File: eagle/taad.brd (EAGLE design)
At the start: 81.2 x 74.3 mm, 49 parts, among them IC1 LD117AS33TR, Q1 16 MHz, X1 MINI-USB-32005-201

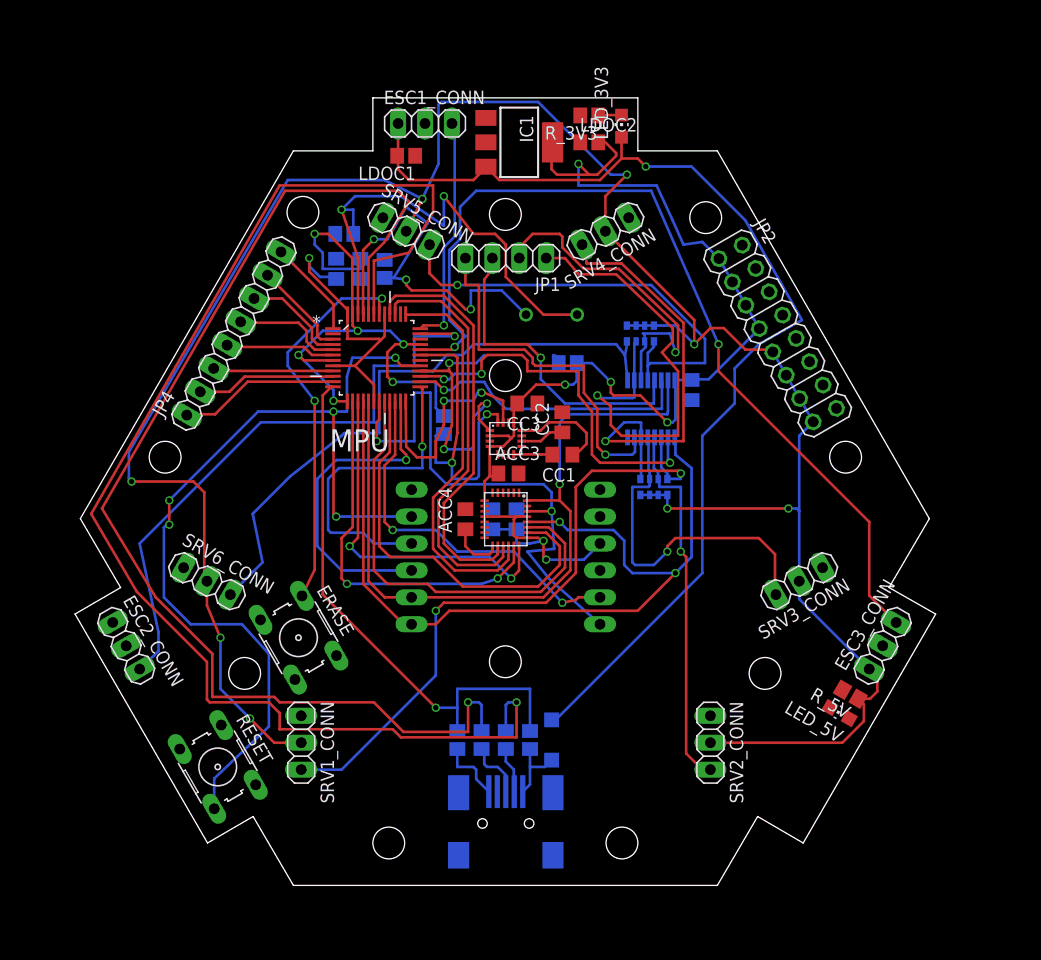
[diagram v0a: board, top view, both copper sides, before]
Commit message: Updated with recommendations from Hannes regarding capacitors on supply and some diagnostic leds. New routing of components
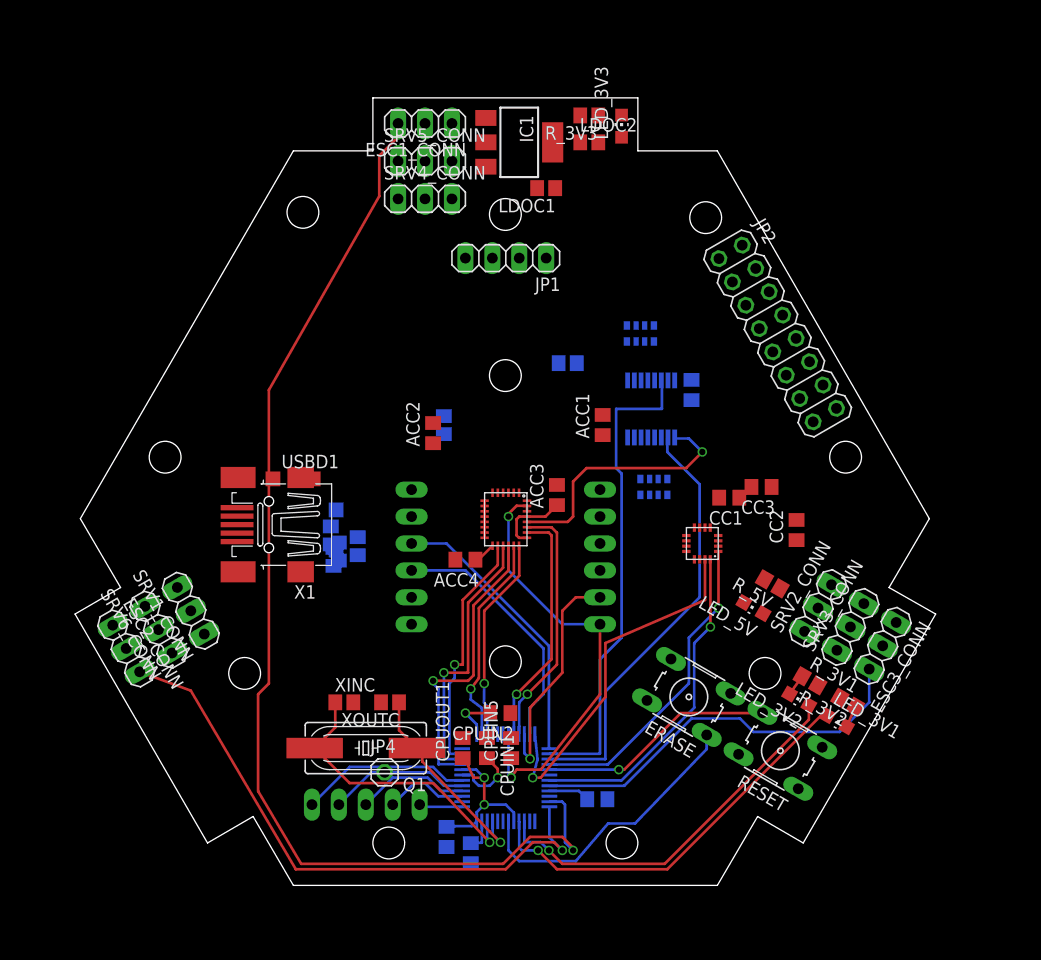
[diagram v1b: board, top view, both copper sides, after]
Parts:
- removed CPUC1: 2.2µ, rcl:C0805
- removed CPUC2: 10µ, rcl:C0805
- added CPUIN1, CPUIN2, CPUIN3, CPUIN4, CPUOUT1: 100n, rcl:C0805
- added CPUIN5: 10µ, rcl:C0805
- added CPUOUT2: 2.2µ, rcl:C0805
- added JP3: (no value), pinhead:1X05
- added LED_3V1, LED_3V2: (no value), led:CHIP-LED0805
- added R_3V1, R_3V2: 160, resistor:R0805
- added USBD1: (no value), diode:SOD123
- JP4: device pinhead:1X08 -> pinhead:1X01
- Q1: device crystal:HC49/S -> crystal:HC49UP
- moved RESET 53.1 mm to (66.5, 12.7), turned to 150 degrees
- moved Q1 44.5 mm to (27.4, 13.0), flipped to the top
- moved XINC 44.2 mm to (25.4, 17.3), flipped to the top
- moved JP4 43.8 mm to (29.2, 10.7), turned to 0 degrees
- moved MPU 41.5 mm to (40.6, 10.2), flipped to the bottom, turned to 180 degrees
- moved XOUTC 40.9 mm to (29.7, 17.3), flipped to the top, turned to 180 degrees
- moved ERASE 37.3 mm to (57.9, 17.8), turned to 150 degrees
- moved X1 36.0 mm to (18.3, 34.0), flipped to the top, turned to 180 degrees
- moved USBD 28.4 mm to (24.6, 33.5)
- moved USBR3 24.5 mm to (26.7, 32.0)
- moved CC2 24.3 mm to (68.1, 33.5)
- moved USBR2 24.0 mm to (24.1, 33.0)
- moved USBR1 23.7 mm to (24.4, 31.0)
- moved CC3 23.5 mm to (64.8, 37.6)
- moved COMPASS 21.0 mm to (59.2, 32.3), turned to 180 degrees
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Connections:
- removed net AD0: JP4.3, MPU.9
- removed net AD1: JP4.2, MPU.10
- removed net AD2: JP4.1, MPU.11
- new net N$1: ESC1_CONN.1, USBD1.A
- new net N$11: JP4.1, MPU.37
- new net N$2: LED_3V2.A, MPU.39
- new net N$6: LED_3V1.A, MPU.40
- new net N$8: LED_3V2.C, R_3V1.1
- new net N$9: LED_3V1.C, R_3V2.1
- net +3V3: now also CPUIN1.2, CPUIN2.2, CPUIN3.2, CPUIN4.2, CPUIN5.1, ERASE.3; no longer CPUC2.1
- net AD3: now also JP3.4; no longer JP4.7
- net AD4: now also JP3.3; no longer JP4.6
- net AD5: now also JP3.2; no longer JP4.5
- net AD6: now also JP3.1; no longer JP4.4
- net ADVREF: now also JP3.5; no longer JP4.8
- net DEN_G: now also MPU.11; no longer MPU.40
- net ESC1: now also MPU.35; no longer MPU.36
- net ESC2: now also MPU.36; no longer MPU.35
- net GND: now also CPUIN1.1, CPUIN2.1, CPUIN3.1, CPUIN4.1, CPUIN5.2, CPUOUT1.2, CPUOUT2.2, R_3V1.2, R_3V2.2; no longer CPUC1.2, CPUC2.2, ERASE.3
- net INT1_G: now also MPU.9; no longer MPU.37
- net INT2_G: now also MPU.10; no longer MPU.39
- net N$24: now also USBD1.C; no longer ESC1_CONN.1
- net NPCS0: now also GYRO/ACCEL.22; no longer GYRO/ACCEL.23
- net NPCS2: now also GYRO/ACCEL.23; no longer GYRO/ACCEL.22
- net VDDCORE: now also CPUOUT1.1, CPUOUT2.1; no longer CPUC1.1
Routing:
- net +5V: track 224.2 -> 0.00 mm, vias 8 -> 0
- net +3V3: track 171.5 -> 28.9 mm, vias 12 -> 2
- net DDM: track 125.5 -> 0.00 mm, vias 1 -> 0
- net DDP: track 112.2 -> 0.00 mm, vias 1 -> 0
- net N$24: track 103.2 -> 0.00 mm, vias 1 -> 0
- net ESC1: track 21.9 -> 108.5 mm
- net SDA: track 68.9 -> 0.00 mm, vias 1 -> 0
- net RESET: track 87.8 -> 22.3 mm, vias 5 -> 1
- net SRV1: track 61.9 -> 0.00 mm, vias 2 -> 0
- net SRV6: track 58.2 -> 0.00 mm
- net SCK: track 81.8 -> 24.4 mm, vias 2 -> 1
- net USB_CONNECTED: track 52.0 -> 0.00 mm, vias 1 -> 0
- net ESC3: track 85.7 -> 37.6 mm, vias 2 -> 0
- net IO1: track 45.0 -> 0.00 mm, vias 1 -> 0
- net SRV5: track 43.0 -> 0.00 mm, vias 1 -> 0
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
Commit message: Routed everything
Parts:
- removed JP2: (no value), pinhead:2X08
- added JP5, JP6: (no value), pinhead:2X04
- moved TWI_DR 35.1 mm to (64.3, 24.4), turned to 0 degrees
- moved USBR2 29.6 mm to (26.7, 3.56), turned to 270 degrees
- moved TWI_CR 28.8 mm to (64.3, 26.7)
- moved JP4 28.6 mm to (57.7, 7.62)
- moved USBR1 28.2 mm to (23.4, 2.79), turned to 180 degrees
- moved USBD1 25.4 mm to (31.8, 61.2)
- moved X1 20.8 mm to (11.9, 14.2), turned to 30 degrees
- moved CC2 12.9 mm to (55.4, 31.5), turned to 270 degrees
- moved USBR3 10.8 mm to (22.4, 22.1), flipped to the top
- moved USBD 10.4 mm to (25.4, 23.1), flipped to the top
- moved ACC1 10.0 mm to (40.4, 39.9)
- moved CC1 9.54 mm to (53.1, 32.5), turned to 90 degrees
- moved USBR4 5.68 mm to (22.4, 26.4), flipped to the top, turned to 270 degrees
- moved CC3 5.61 mm to (64.3, 32.0)
- moved LED_3V3 5.49 mm to (48.5, 67.1), turned to 270 degrees
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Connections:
- net +3V3: now also JP5.1, JP5.3, JP5.5, JP5.7; no longer JP2.1, JP2.3, JP2.5, JP2.7
- net +5V: now also JP6.1, JP6.3, JP6.5, JP6.7; no longer JP2.11, JP2.13, JP2.15, JP2.9
- net GND: now also JP5.2, JP5.4, JP5.6, JP5.8, JP6.2, JP6.4, JP6.6, JP6.8; no longer JP2.10, JP2.12, JP2.14, JP2.16, JP2.2, JP2.4, JP2.6, JP2.8
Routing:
- net +3V3: track 28.9 -> 208.1 mm, vias 2 -> 8
- net +5V: track 0.00 -> 161.3 mm, vias 0 -> 3
- net SDA: track 0.00 -> 82.9 mm, vias 0 -> 1
- net SRV1: track 0.00 -> 65.6 mm, vias 0 -> 1
- net SRV6: track 0.00 -> 65.3 mm, vias 0 -> 3
- net N$24: track 0.00 -> 64.7 mm
- net SCK: track 24.4 -> 81.7 mm, vias 1 -> 2
- net RESET: track 22.3 -> 72.0 mm
- net SRV4: track 0.00 -> 45.6 mm, vias 0 -> 2
- net IO3: track 0.00 -> 35.3 mm
- net SRV3: track 0.00 -> 34.9 mm, vias 0 -> 1
- net SRV5: track 0.00 -> 33.7 mm
- net VDDCORE: track 16.9 -> 44.2 mm, vias 2 -> 4
- net SRV2: track 0.00 -> 26.6 mm, vias 0 -> 1
- net IO4: track 0.00 -> 26.4 mm, vias 0 -> 1
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- added copper zone on layer 1, net GND
- added copper zone on layer 16, net GND

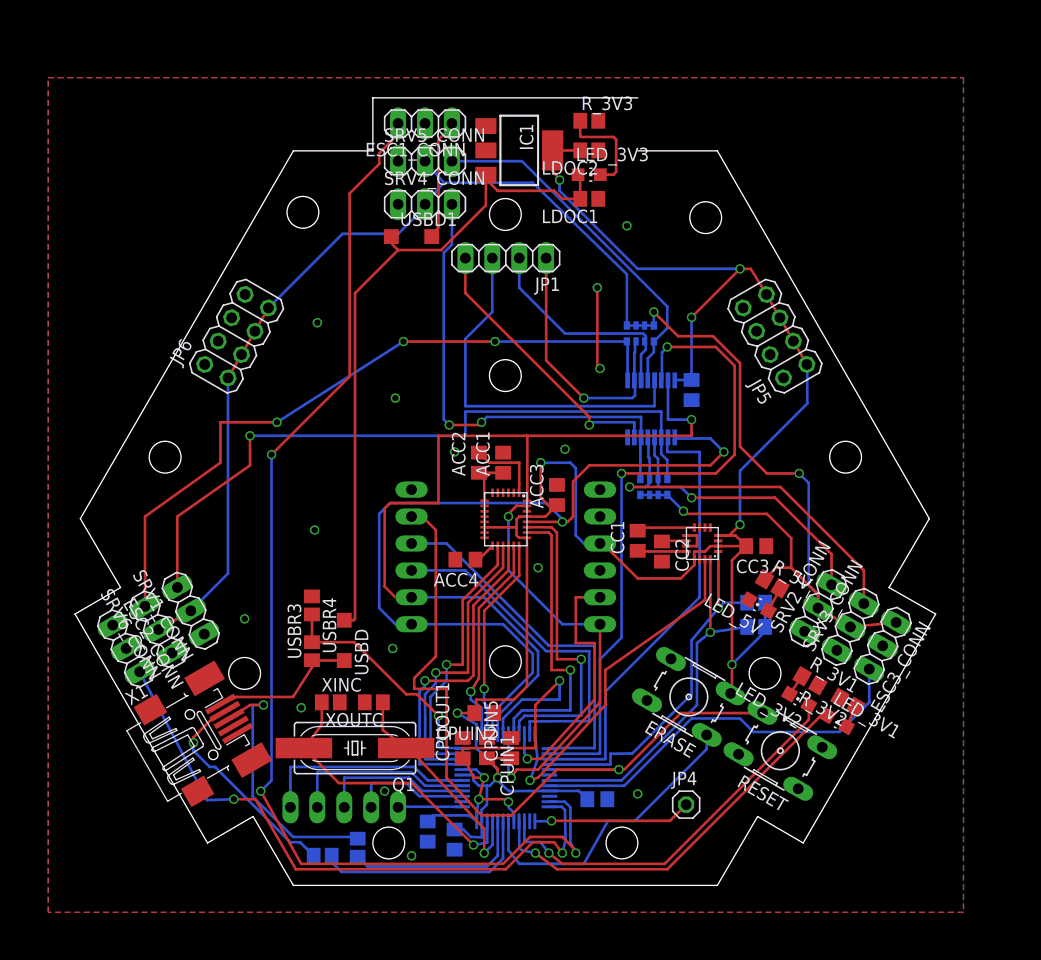
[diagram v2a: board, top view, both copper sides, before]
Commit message: Increased isolation to 16mil
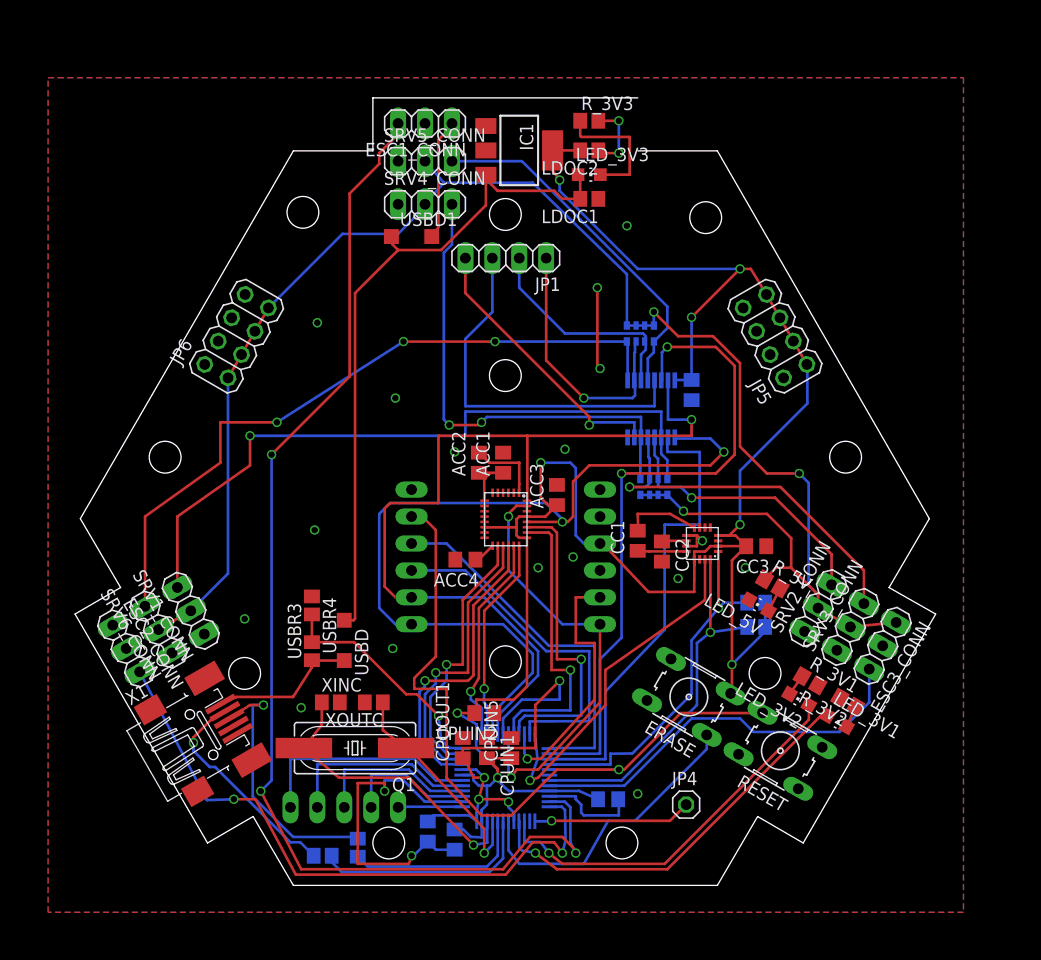
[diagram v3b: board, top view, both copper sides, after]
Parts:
- moved CPUIN3 1.02 mm to (50.3, 8.13)
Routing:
- net GND: track 17.8 -> 66.9 mm, vias 11 -> 21
- net +3V3: track 208.1 -> 211.5 mm
- net N$5: track 9.61 -> 12.4 mm
- net NPCS3: track 42.4 -> 44.2 mm
- net N$25: track 5.60 -> 7.28 mm
- net INT1_G: track 30.6 -> 29.4 mm
- net AD6: track 20.5 -> 21.6 mm
- net AD5: track 17.5 -> 18.6 mm
- net AD4: track 14.4 -> 15.5 mm
- net AD3: track 11.4 -> 12.5 mm
- net INT2_G: track 28.4 -> 27.4 mm
- net DEN_G: track 26.1 -> 25.2 mm
- net ESC1: track 110.5 -> 111.4 mm
- net ESC2: track 58.3 -> 59.1 mm
- net USB_CONNECTED: track 22.6 -> 22.1 mm

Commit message: Simplified form of PCB. Rerouted everything
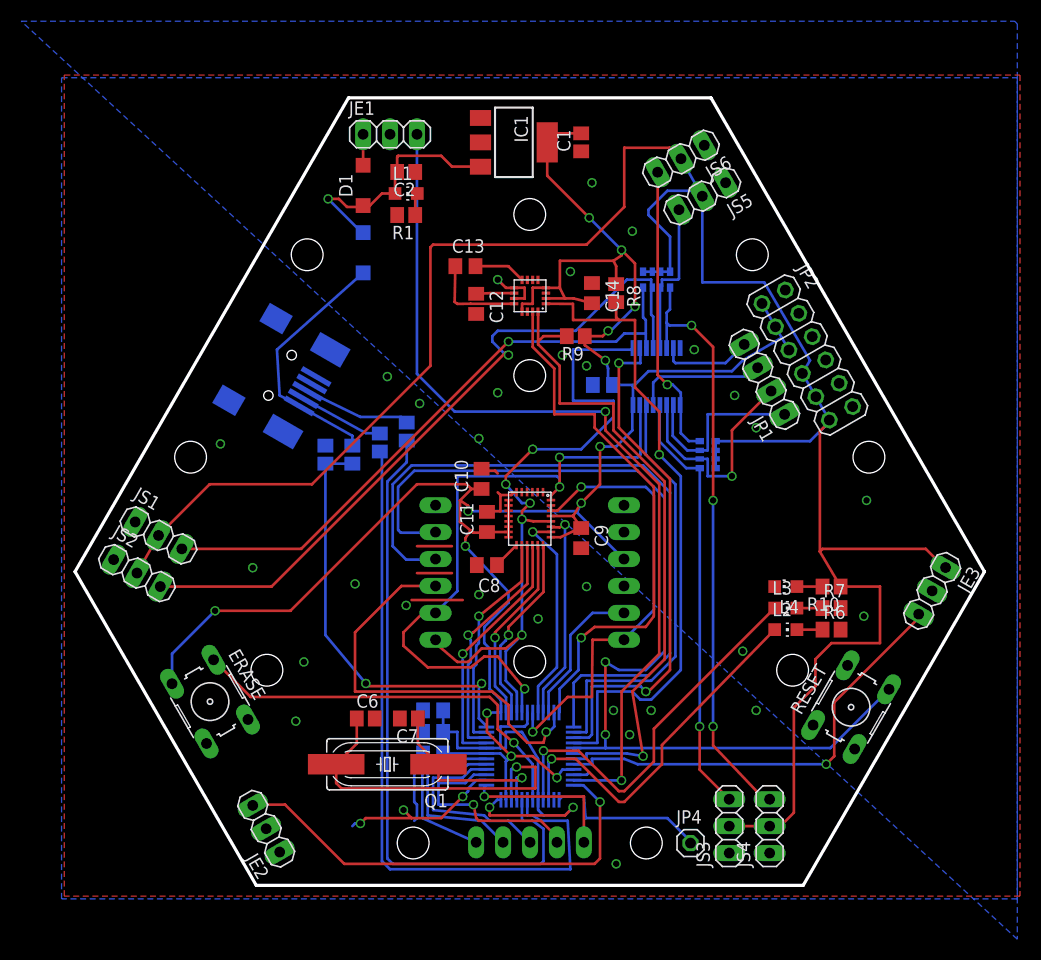
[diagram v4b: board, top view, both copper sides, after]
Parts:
- removed ACC1, ACC3, CPUIN1, CPUIN2, CPUIN3, CPUIN4, CPUOUT1: 100n, rcl:C0805
- removed ACC2, CPUIN5, PWMC: 10µ, rcl:C0805
- removed ACC4: 10n, rcl:C0805
- removed CC1: 0.22µ, rcl:C0805
- removed CC2: 4.7µ, rcl:C0805
- removed CC3: 0.1µ, rcl:C0805
- removed CPUOUT2: 2.2µ, rcl:C0805
- removed ESC1_CONN, ESC2_CONN, ESC3_CONN, SRV1_CONN, SRV2_CONN, SRV3_CONN, SRV4_CONN, SRV5_CONN, SRV6_CONN: (no value), pinhead:1X03
- removed JP5, JP6: (no value), pinhead:2X04
- removed LDOC1, LDOC2: 100n, resistor:C0805
- removed LED_3V1, LED_3V2, LED_3V3, LED_5V: (no value), led:CHIP-LED0805
- removed R_3V1, R_3V2, R_3V3, R_5V: 160, resistor:R0805
- removed TWI_CR, TWI_DR: 2.2k, resistor:R0805
- removed USBD, USBD1: (no value), diode:SOD123
- removed USBR1, USBR2: 27, resistor:R0805
- removed USBR3: 27k, resistor:R0805
- removed USBR4: 47k, resistor:R0805
- removed XINC, XOUTC: 10p, resistor:C0805
- added 2, D1: (no value), diode:SOD123
- added C1, C2: 100n, resistor:C0805
- added C10, C4, C9: 100n, rcl:C0805
- added C11, C15, C3: 10µ, rcl:C0805
- added C12: 4.7µ, rcl:C0805
- added C13: 0.22µ, rcl:C0805
- added C14: 0.1µ, rcl:C0805
- added C5: 2.2µ, rcl:C0805
- added C6, C7: 10p, resistor:C0805
- added C8: 10n, rcl:C0805
- added JE1, JE2, JE3, JS1, JS2, JS3, JS4, JS5, JS6: (no value), pinhead:1X03
- added JP2: (no value), pinhead:2X06
- added L1, L2, L3, L4: (no value), led:CHIP-LED0805
- added R1, R10, R6, R7: 160, resistor:R0805
- added R2, R3: 27, resistor:R0805
- added R4: 27k, resistor:R0805
- added R5: 47k, resistor:R0805
- added R8, R9: 2.2k, resistor:R0805
- X1: value MINI-USB-32005-201 -> (none)
- moved ERASE 45.2 mm to (12.7, 17.3), turned to 300 degrees
- moved X1 34.7 mm to (19.3, 48.1), flipped to the bottom, turned to 210 degrees
- moved COMPASS 28.5 mm to (42.9, 55.6)
- moved JP1 26.9 mm to (65.0, 47.7), turned to 120 degrees
- moved RN1 19.6 mm to (54.9, 57.1), turned to 0 degrees
- moved JP3 17.8 mm to (42.9, 4.06)
- moved RN2 13.1 mm to (59.7, 40.6), turned to 90 degrees
- moved RESET 7.84 mm to (73.2, 16.8), turned to 60 degrees
- moved JP4 3.65 mm to (58.1, 3.99)
- moved Q1 3.41 mm to (29.5, 11.4)
- moved I/O-PWM 3.09 mm to (54.9, 48.0), turned to 180 degrees
- moved MPU 3.06 mm to (42.9, 12.2)
- moved RF 2.69 mm to (42.9, 29.5)
- moved GYRO/ACCEL 2.26 mm to (42.9, 34.6)
- moved IC1 0.92 mm to (41.4, 70.1)
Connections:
- net +3V3: now also C1.2, C10.1, C11.1, C14.2, C15.1, C3.1, C9.1, JP2.1, JP2.3, JP2.5, R8.1, R9.1; no longer ACC1.1, ACC2.1, ACC3.1, CC3.2, CPUIN1.2, CPUIN2.2, CPUIN3.2, CPUIN4.2, CPUIN5.1, JP5.1, JP5.3, JP5.5, JP5.7, LDOC2.2, PWMC.1, TWI_CR.1, TWI_DR.1
- net +5V: now also JE3.1, JP2.11, JP2.7, JP2.9, JS1.2, JS2.2, JS3.2, JS4.2, JS5.2, JS6.2, R10.1; no longer ESC3_CONN.1, JP6.1, JP6.3, JP6.5, JP6.7, R_5V.1, SRV1_CONN.2, SRV2_CONN.2, SRV3_CONN.2, SRV4_CONN.2, SRV5_CONN.2, SRV6_CONN.2
- net DDM: now also R2.2; no longer USBR1.2
- net DDP: now also R3.2; no longer USBR2.2
- net ESC1: now also JE1.3; no longer ESC1_CONN.3
- net ESC2: now also JE2.3; no longer ESC2_CONN.3
- net ESC3: now also JE3.3; no longer ESC3_CONN.3
- net GND: now also C1.1, C10.2, C11.2, C12.2, C14.1, C15.2, C2.1, C3.2, C4.2, C5.2, C6.2, C7.2, C8.2, C9.2, JE1.2, JE2.2, JE3.2, JP2.10, JP2.12, JP2.2, JP2.4, JP2.6, JP2.8, JS1.1, JS2.1, JS3.1, JS4.1, JS5.1, JS6.1, L4.C, R1.2, R5.1, R6.2, R7.2; no longer ACC1.2, ACC2.2, ACC3.2, ACC4.2, CC2.2, CC3.1, CPUIN1.1, CPUIN2.1, CPUIN3.1, CPUIN4.1, CPUIN5.2, CPUOUT1.2, CPUOUT2.2, ESC1_CONN.2, ESC2_CONN.2, ESC3_CONN.2, JP5.2, JP5.4, JP5.6, JP5.8, JP6.2, JP6.4, JP6.6, JP6.8, LDOC1.1, LDOC2.1, LED_5V.C, PWMC.2, R_3V1.2, R_3V2.2, R_3V3.2, SRV1_CONN.1, SRV2_CONN.1, SRV3_CONN.1, SRV4_CONN.1, SRV5_CONN.1, SRV6_CONN.1, USBR4.1, XINC.2, XOUTC.2
- net N$1: now also D1.A, JE1.1; no longer ESC1_CONN.1, USBD1.A
- net N$2: now also L2.A; no longer LED_3V2.A
- net N$24: now also 2.C, C2.2, D1.C, L1.A; no longer LDOC1.2, LED_3V3.A, USBD.C, USBD1.C
- net N$25: now also C13.2; no longer CC1.2
- net N$3: now also R3.1; no longer USBR2.1
- net N$32: now also C13.1; no longer CC1.1
- net N$33: now also C12.1; no longer CC2.1
- net N$34: now also C8.1; no longer ACC4.1
- net N$4: now also R2.1; no longer USBR1.1
- net N$5: now also L1.C, R1.1; no longer LED_3V3.C, R_3V3.1
- net N$6: now also L3.A; no longer LED_3V1.A
- net N$7: now also L4.A, R10.2; no longer LED_5V.A, R_5V.2
- net N$8: now also L2.C, R6.1; no longer LED_3V2.C, R_3V1.1
- net N$9: now also L3.C, R7.1; no longer LED_3V1.C, R_3V2.1
- net SRV1: now also JS1.3; no longer SRV1_CONN.3
- net SRV2: now also JS2.3; no longer SRV2_CONN.3
- net SRV3: now also JS5.3; no longer SRV3_CONN.3
- net SRV4: now also JS4.3; no longer SRV4_CONN.3
- net SRV5: now also JS3.3; no longer SRV5_CONN.3
- net SRV6: now also JS6.3; no longer SRV6_CONN.3
- net TWI_CLOCK: now also R8.2; no longer TWI_CR.2
- net TWI_DATA: now also R9.2; no longer TWI_DR.2
- net USB+5V: now also 2.A, R4.1; no longer USBD.A, USBR3.1
- net USB_CONNECTED: now also R4.2, R5.2; no longer USBR3.2, USBR4.2
- net VDDCORE: now also C4.1, C5.1; no longer CPUOUT1.1, CPUOUT2.1
- net XIN: now also C6.1; no longer XINC.1
- net XOUT: now also C7.1; no longer XOUTC.1
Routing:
- net +5V: track 161.3 -> 208.4 mm, vias 3 -> 0
- net DDM: track 21.2 -> 66.8 mm
- net DDP: track 17.3 -> 62.5 mm
- net SRV2: track 26.6 -> 68.5 mm
- net N$24: track 64.7 -> 23.7 mm, vias 0 -> 1
- net SRV6: track 65.3 -> 28.0 mm, vias 3 -> 1
- net RF_WAKE: track 35.3 -> 68.0 mm
- net TWI_CLOCK: track 34.1 -> 62.9 mm
- net ESC1: track 111.4 -> 84.8 mm, vias 3 -> 2
- net TWI_DATA: track 34.7 -> 61.2 mm
- net RESET: track 72.0 -> 95.7 mm, vias 1 -> 2
- net IO3: track 35.3 -> 12.6 mm
- net PWM_CLOCK: track 62.4 -> 40.3 mm, vias 2 -> 0
- net SRV3: track 34.9 -> 14.7 mm, vias 1 -> 0
- net SDA: track 82.9 -> 63.0 mm, vias 1 -> 3
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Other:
- board size 81.2 x 74.3 mm -> 85.8 x 74.3 mm
